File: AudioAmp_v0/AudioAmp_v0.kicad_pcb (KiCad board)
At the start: 2 copper layers, 95 x 72 mm, 82 parts, among them J1 AudioJack3, J2 Conn_01x02_Pin, J3 Connector_RCJ-042, J4 Connector_RCJ-042, J5 AudioJack3, J6 Conn_01x02_Pin, J7 Conn_01x02_Pin, Q1 NMOS_ MTB7D0N6RJ3, Q2 PMOS_MTP4835I3, Q3 NMOS_BSS138, Q4 PMOS_BSS84, Q5 PMOS_BSS84, Q6 PMOS_MTP4835I3, Q7 NMOS_BSS138, Q8 NMOS_ MTB7D0N6RJ3, SW1 SW_DPDT_x2, SW2 SW_DPDT_x2, U1 MAU108, U2 NJM5532, U3 NJM5532

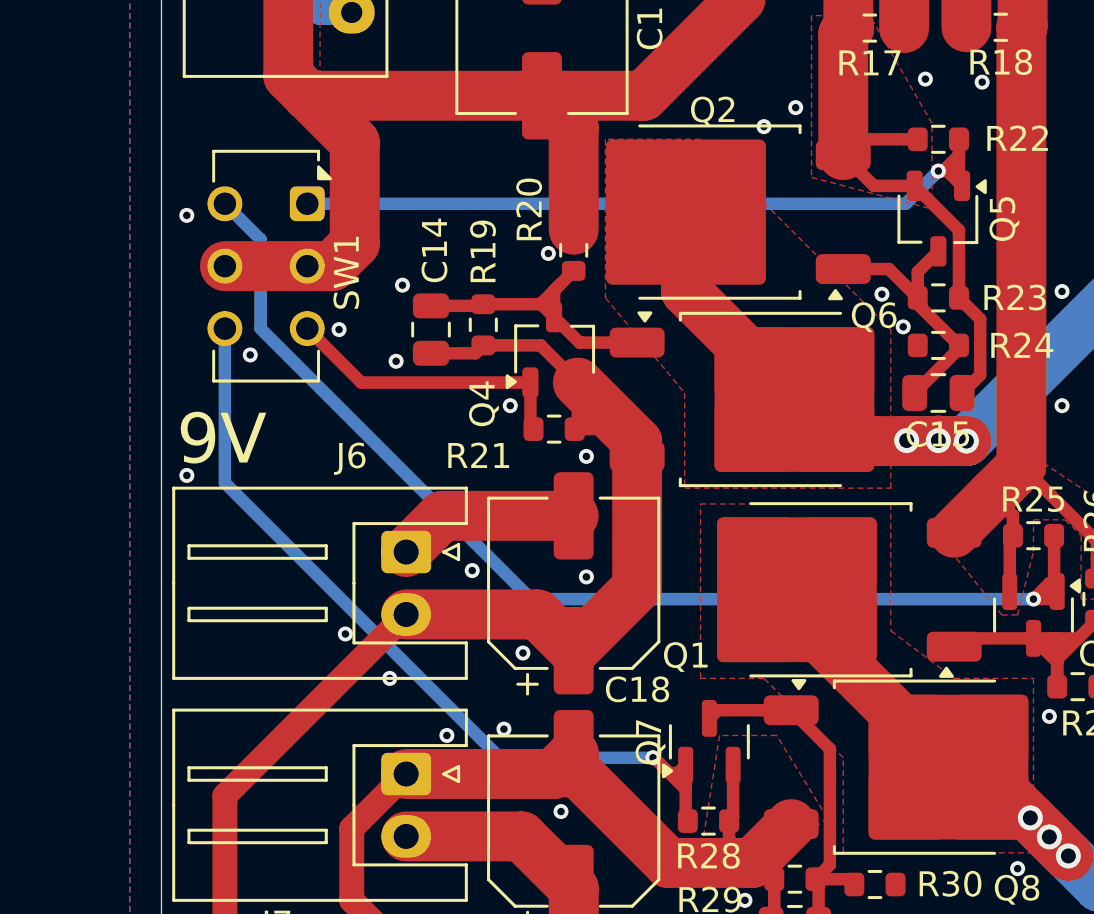
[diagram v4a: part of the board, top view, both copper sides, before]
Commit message: スイッチの方向修正
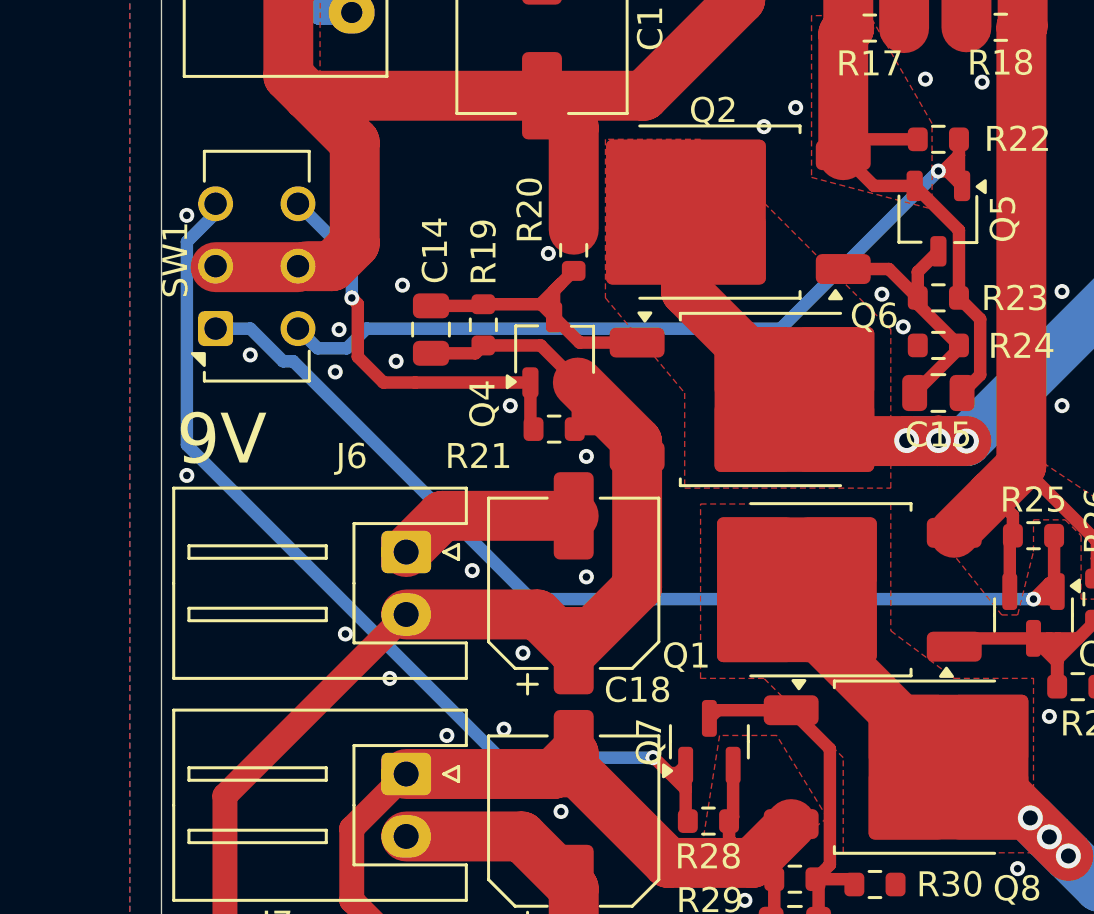
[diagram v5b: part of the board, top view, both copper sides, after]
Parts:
- moved SW1 6.20 mm to (2.17, 27.9), turned to 90 degrees
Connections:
- SW1 pad 1: Net-(Q5-G) -> Net-(Q3-G)
- SW1 pad 3: Net-(Q4-G) -> Net-(Q7-G)
- SW1 pad 4: Net-(Q3-G) -> Net-(Q5-G)
- SW1 pad 6: Net-(Q7-G) -> Net-(Q4-G)
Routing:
- net Net-(Q7-G): track 32.8 -> 38.9 mm
- net Net-(Q4-G): track 11.7 -> 16.4 mm, vias 0 -> 1
- net Net-(Q3-G): track 45.5 -> 41.7 mm
- net Net-(Q5-G): track 30.0 -> 33.1 mm
- net GND: vias 101 -> 102

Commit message: ビア打ち
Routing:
- net VEE: track 107.2 -> 97.6 mm
- net VCC: track 107.2 -> 97.8 mm
- net Net-(Q1-G): track 14.6 -> 16.3 mm
- net GND: vias 102 -> 126
